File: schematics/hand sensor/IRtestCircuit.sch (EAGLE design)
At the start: 5 parts, among them IC1 AD746N, T1 BPX81

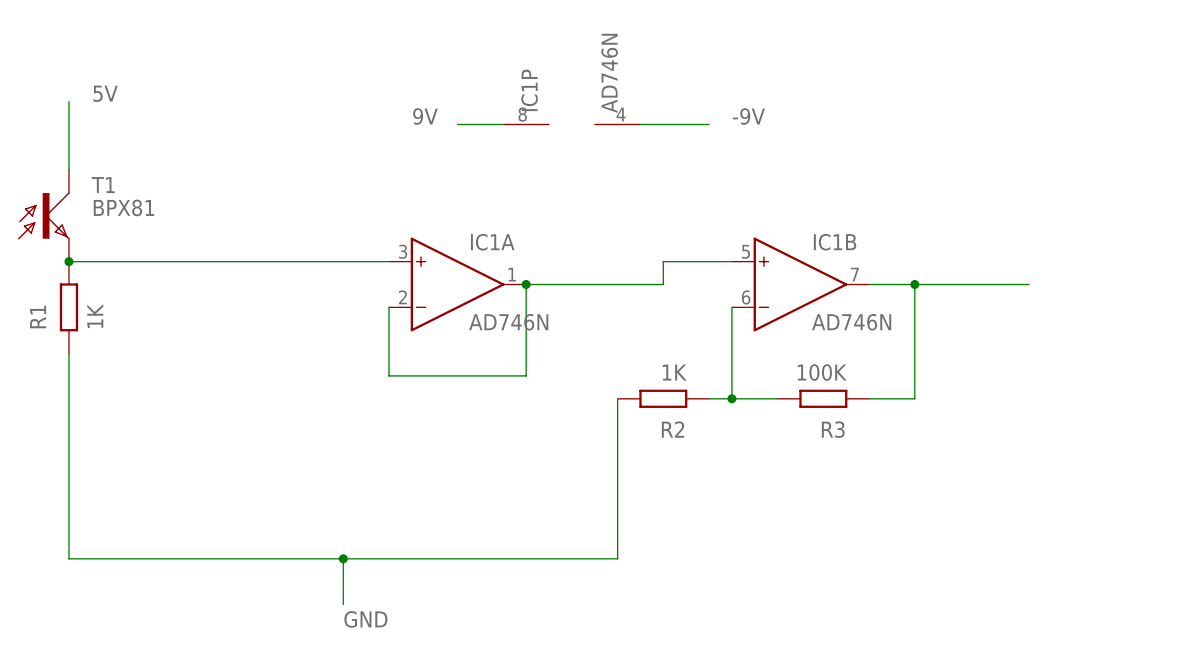
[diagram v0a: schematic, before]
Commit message: Implement socket transfering
Implement socket transfering between Python and Unity.
Arduino now has IR sensor implemented.
Record 10 signal from sensor (before fix).
Implement and train several models.
Implement data analytic module.
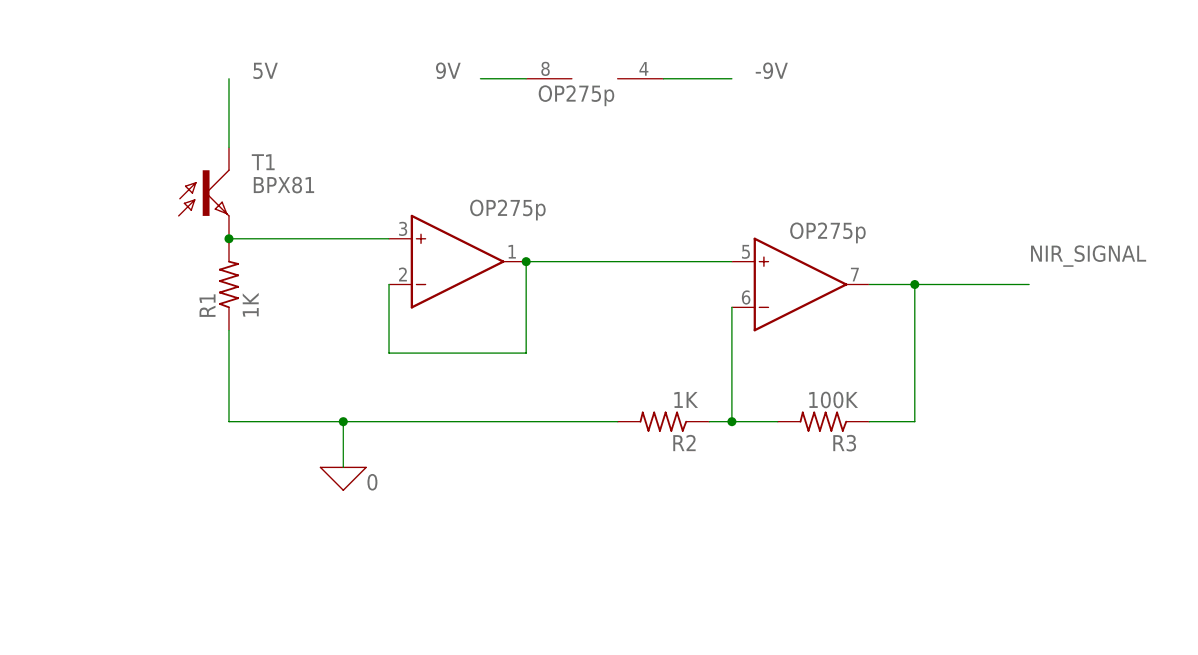
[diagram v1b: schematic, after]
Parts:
- IC1: value AD746N -> OP275p
- R1, R2, R3: device ngspice-simulation:R -> rcl:R-US_0207/10
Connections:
- net GND renamed 0
- net N$5 renamed NIR_SIGNAL
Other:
- moved on the sheet: T1
